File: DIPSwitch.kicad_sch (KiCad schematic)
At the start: 9 parts

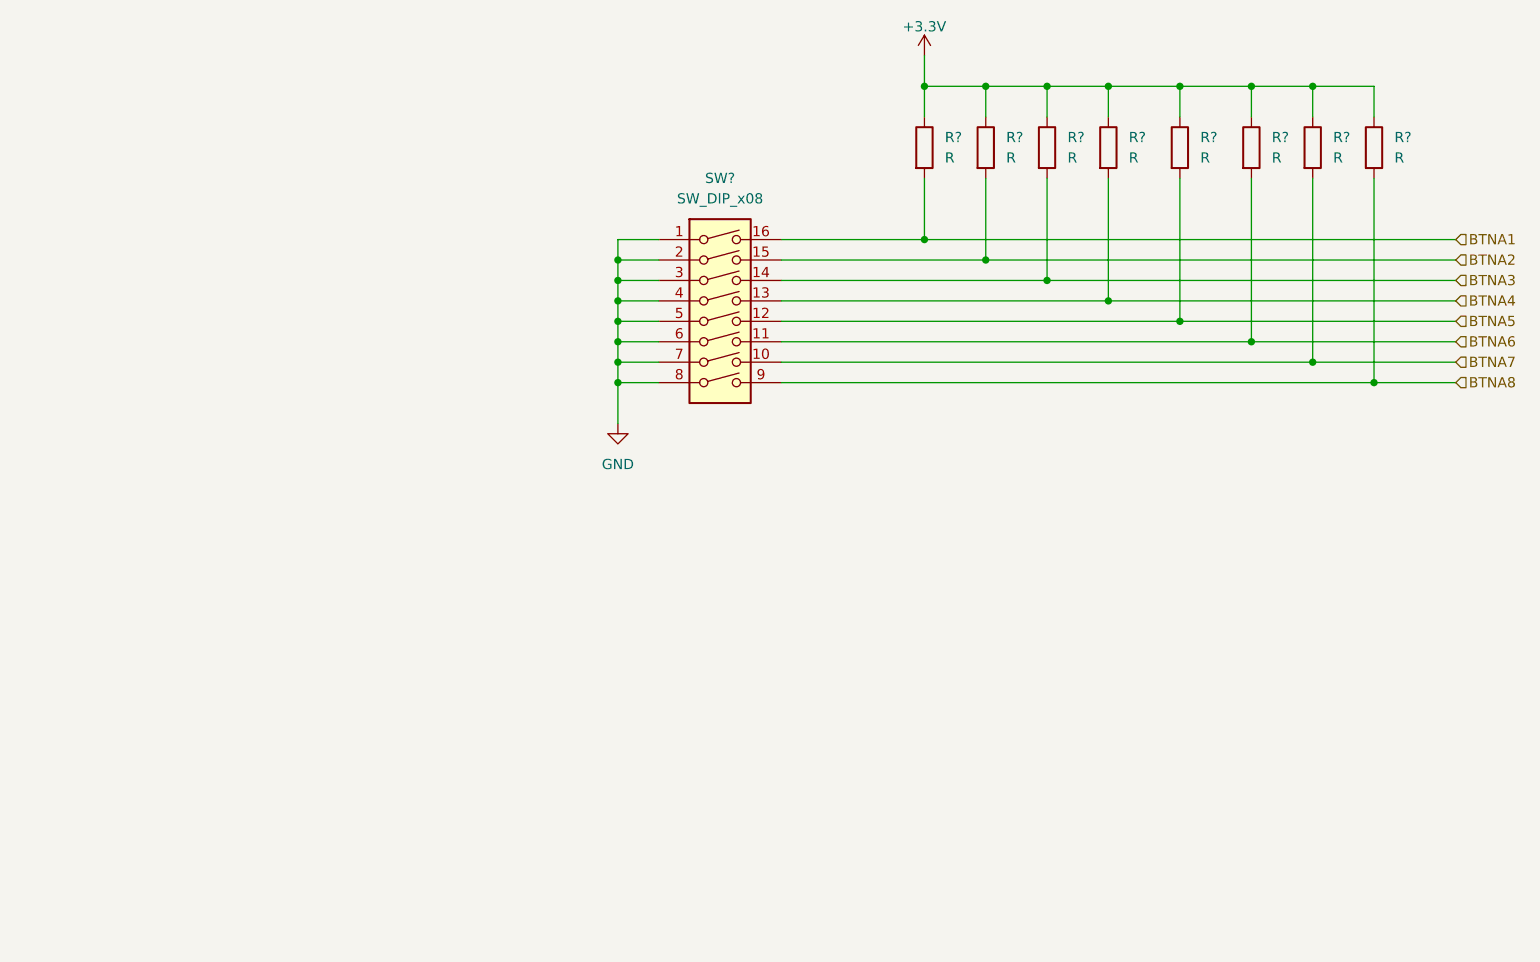
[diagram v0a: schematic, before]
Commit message: Adicionado o circuito de Debounce.
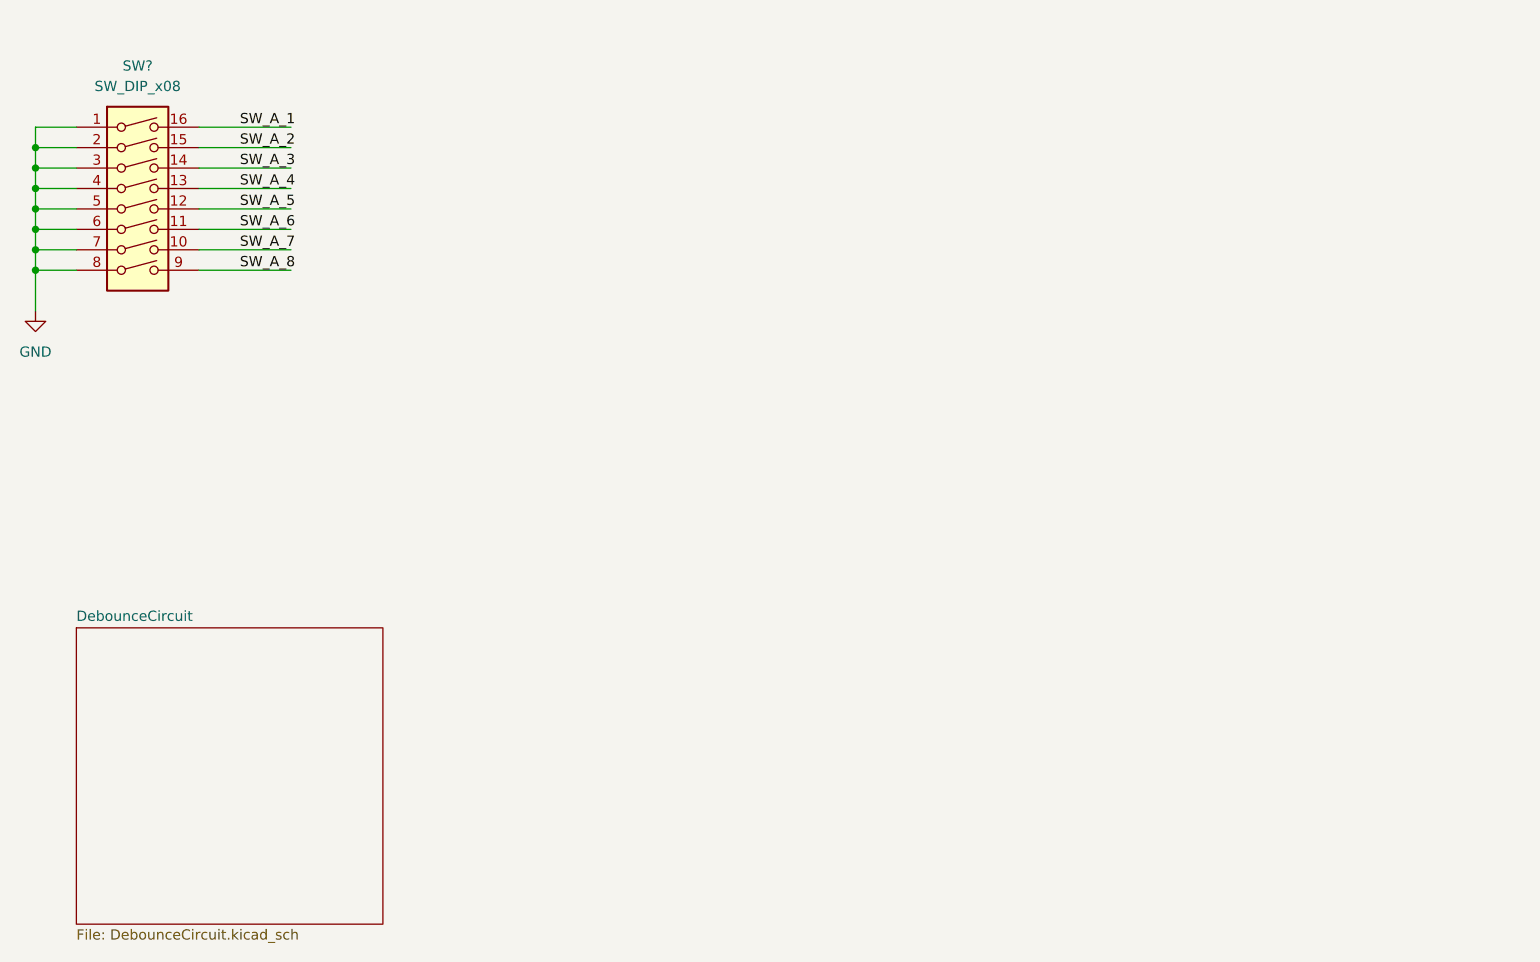
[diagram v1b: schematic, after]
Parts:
- removed R? (x8): R, symbol Device:R
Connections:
- net BTNA1 renamed SW_A_1
- net BTNA2 renamed SW_A_2
- net BTNA3 renamed SW_A_3
- net BTNA4 renamed SW_A_4
- net BTNA5 renamed SW_A_5
- net BTNA6 renamed SW_A_6
- net BTNA7 renamed SW_A_7
- net BTNA8 renamed SW_A_8
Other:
- added sheet DebounceCircuit (DebounceCircuit.kicad_sch)
- moved on the sheet: SW?
